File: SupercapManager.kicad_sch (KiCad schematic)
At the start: 7 parts, among them J1 JST4_M, J2 XT30_M, J3 XT30_M, J4 XT30_M, J5 XT30_M, Q11 BSC015NE2LS5I, Q12 BSC015NE2LS5I

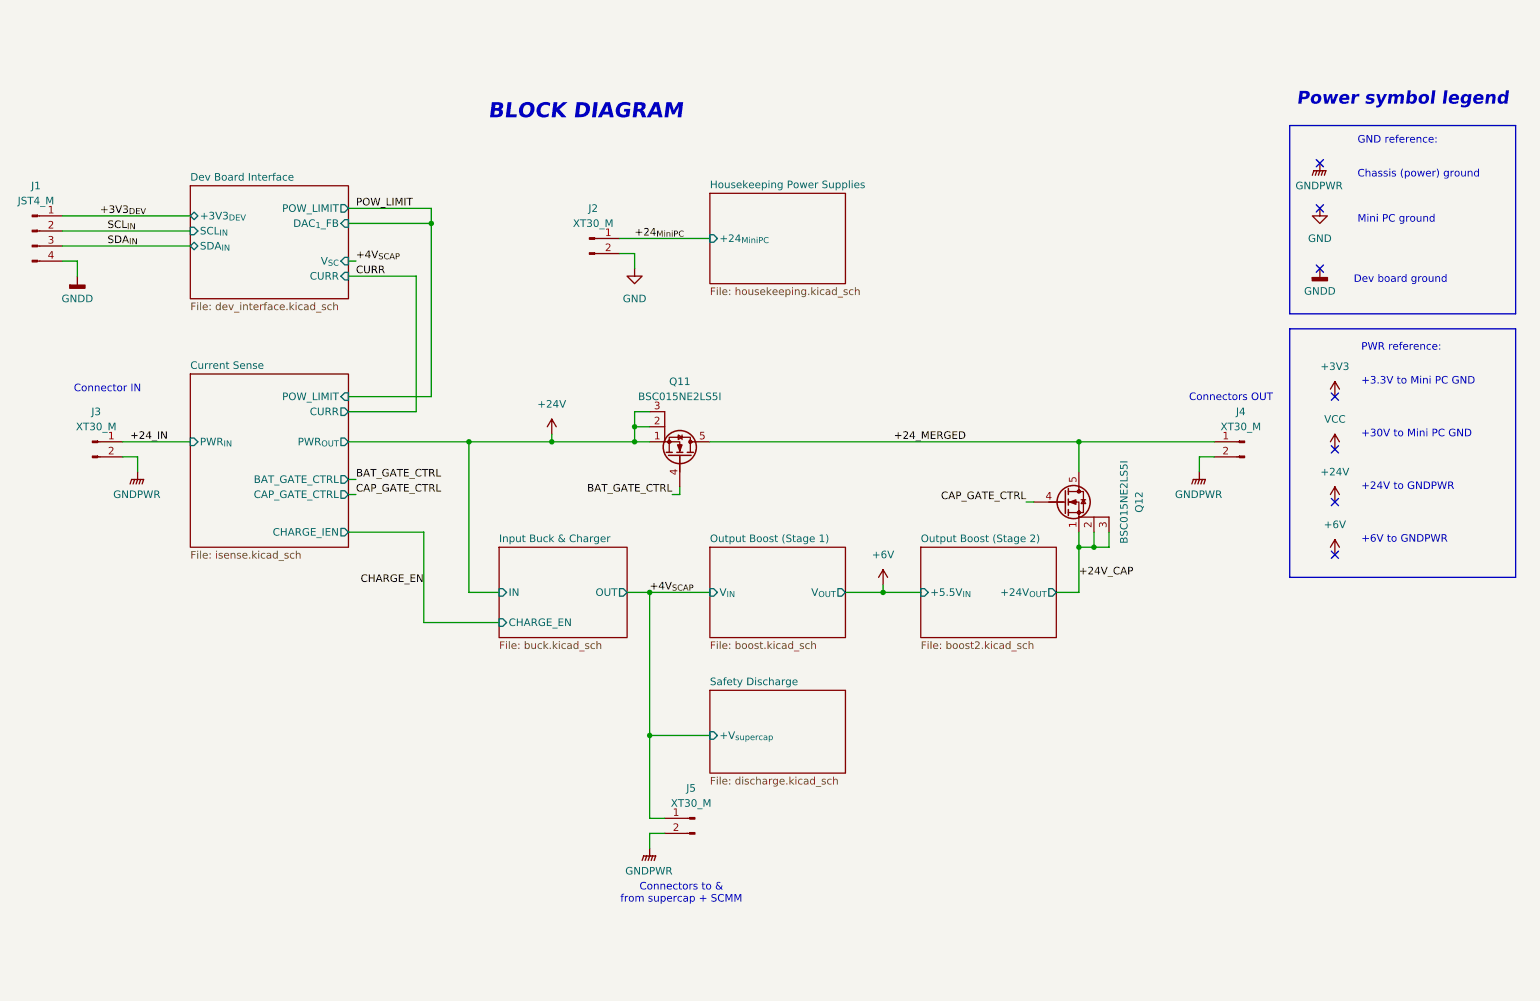
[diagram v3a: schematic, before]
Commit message: Up charging current to 6A
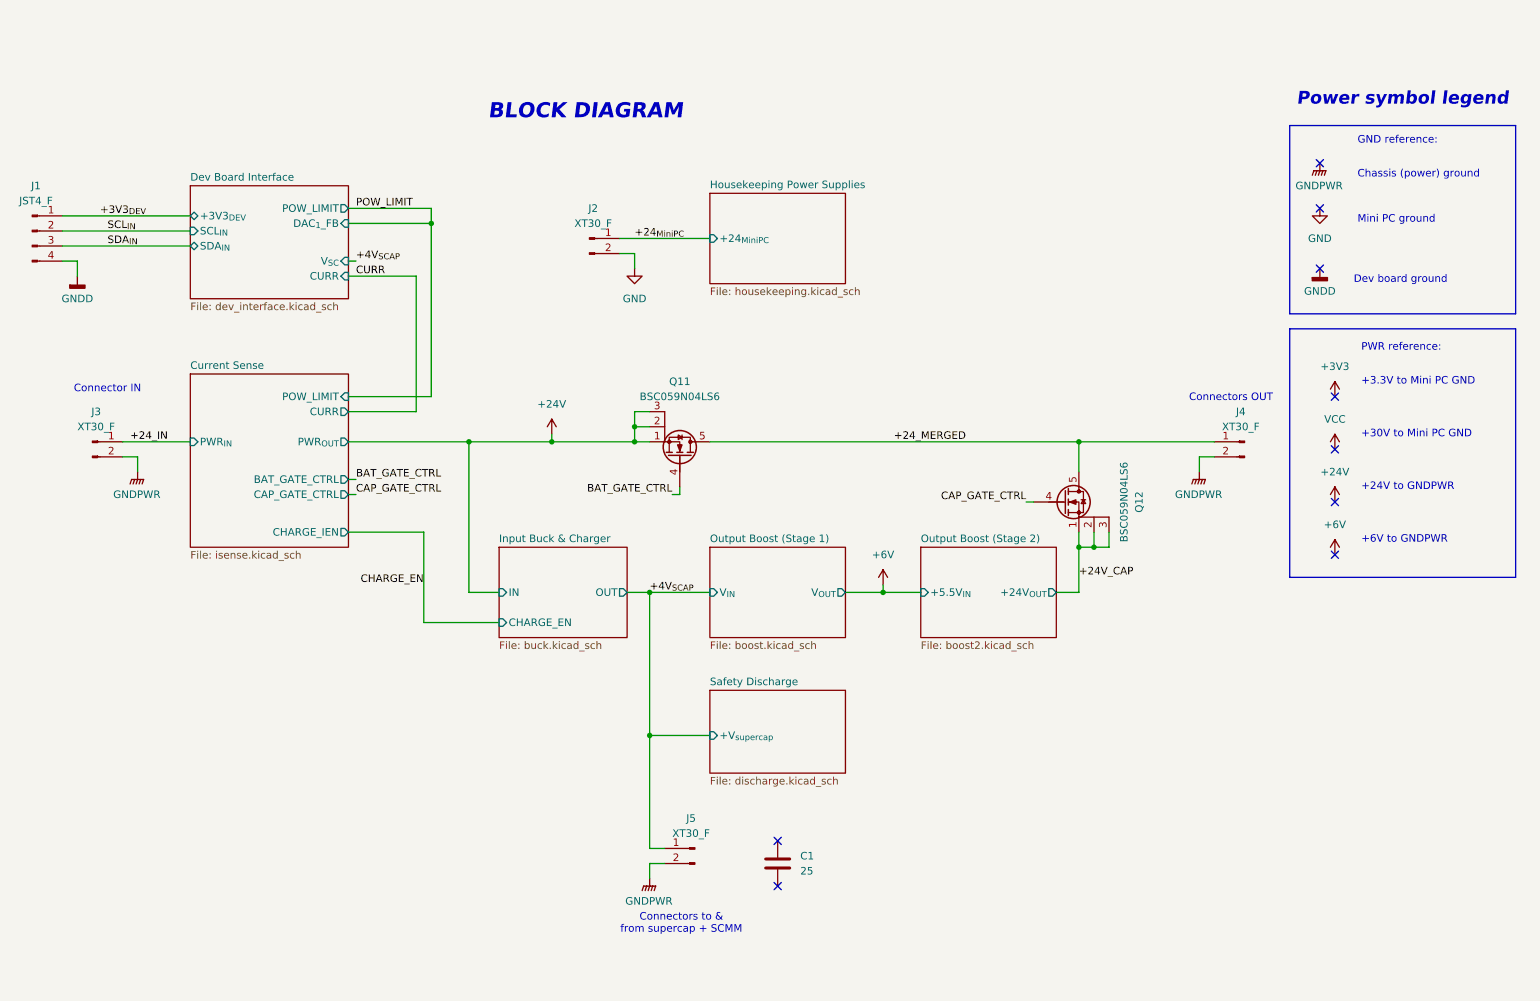
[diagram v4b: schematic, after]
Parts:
- added C1: 25, symbol Device:C
- J1: value JST4_M -> JST4_F
- J2, J3, J4, J5: value XT30_M -> XT30_F; footprint Connector_AMASS:AMASS_XT30U-M_1x02_P5.0mm_Vertical -> Connector_AMASS:AMASS_XT30U-F_1x02_P5.0mm_Vertical
- Q11, Q12: value BSC015NE2LS5I -> BSC059N04LS6; Mouser Part Number 726-BSC015NE2LS5IATM -> 726-BSC059N04LS6ATMA
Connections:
- no-connect marks 7 -> 9
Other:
- moved on the sheet: J5
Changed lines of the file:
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@@
 	(text "Connectors to &\nfrom supercap + SCMM"
 		(exclude_from_sim no)
-		(at 131.064 168.402 0)
+		(at 131.064 173.482 0)
 		(effects
 			(font
@@
 	)
 	(no_connect
+		(at 147.32 161.29)
+	)
+	(no_connect
 		(at 241.3 86.36)
+	)
+	(no_connect
+		(at 147.32 168.91)
 	)
 	(no_connect
@@
 	(wire
 		(pts
-			(xy 128.27 160.02) (xy 125.73 160.02)
+			(xy 128.27 165.1) (xy 125.73 165.1)
 		)
 		(stroke
@@
 	(wire
 		(pts
-			(xy 125.73 157.48) (xy 125.73 143.51)
+			(xy 125.73 162.56) (xy 125.73 143.51)
 		)
 		(stroke
@@
 	(wire
 		(pts
-			(xy 128.27 157.48) (xy 125.73 157.48)
+			(xy 128.27 162.56) (xy 125.73 162.56)
 		)
 		(stroke
@@
 	(wire
 		(pts
-			(xy 125.73 160.02) (xy 125.73 162.56)
+			(xy 125.73 165.1) (xy 125.73 167.64)
 		)
 		(stroke
@@
 			)
 		)
-		(property "Value" "BSC015NE2LS5I"
+		(property "Value" "BSC059N04LS6"
 			(at 130.81 86.36 90)
 			(effects
@@
 			)
 		)
-		(property "Mouser Part Number" "726-BSC015NE2LS5IATM"
+		(property "Mouser Part Number" "726-BSC059N04LS6ATMA"
 			(at 130.81 96.52 0)
 			(effects
@@
 	)
 	(symbol
+		(lib_id "Device:C")
+		(at 147.32 165.1 0)
+		(unit 1)
+		(exclude_from_sim no)
+		(in_bom yes)
+		(on_board no)
+		(dnp no)
+		(fields_autoplaced yes)
+		(property "Reference" "C1"
+			(at 151.13 163.8299 0)
+			(effects
+				(font
+					(size 1.27 1.27)
+				)
+				(justify left)
+			)
+		)
+		(property "Value" "25"
+			(at 151.13 166.3699 0)
+			(effects
+				(font
+					(size 1.27 1.27)
+				)
+				(justify left)
+			)
+		)
+		(property "Footprint" ""
+			(at 148.2852 168.91 0)
+			(effects
+				(font
+					(size 1.27 1.27)
+				)
+				(hide yes)
+			)
+		)
+		(property "Datasheet" "https://www.mouser.com/datasheet/2/40/AVX_SCC-3084824.pdf"
+			(at 147.32 165.1 0)
+			(effects
+				(font
+					(size 1.27 1.27)
+				)
+				(hide yes)
+			)
+		)
+		(property "Description" "Supercapacitor"
+			(at 147.32 165.1 0)
+			(effects
+				(font
+					(size 1.27 1.27)
+				)
+				(hide yes)
+			)
+		)
+		(property "Mouser Part Number" "581-SCCU25B256SRB"
+			(at 147.32 165.1 0)
+			(effects
+				(font
+					(size 1.27 1.27)
+				)
+				(hide yes)
+			)
+		)
+		(pin "1"
+		)
+		(pin "2"
+		)
+		(instances
+			(project ""
+				(path "/6197145b-e7d4-44cc-9d90-537b6501bf60"
+					(reference "C1")
+					(unit 1)
+				)
+			)
+		)
+	)
+	(symbol
 		(lib_id "power:VCC")
 		(at 241.3 95.25 0)
@@
 	(symbol
 		(lib_id "Connector:Conn_01x02_Pin")
-		(at 133.35 157.48 0)
+		(at 133.35 162.56 0)
 		(mirror y)
 		(unit 1)
@@
 		(dnp no)
 		(property "Reference" "J5"
-			(at 132.715 152.4 0)
-			(effects
-				(font
-					(size 1.27 1.27)
-				)
-			)
-		)
-		(property "Value" "XT30_M"
-			(at 132.715 154.94 0)
-			(effects
-				(font
-					(size 1.27 1.27)
-				)
-			)
-		)
-		(property "Footprint" "Connector_AMASS:AMASS_XT30U-M_1x02_P5.0mm_Vertical"
-			(at 133.35 157.48 0)
+			(at 132.715 157.48 0)
+			(effects
+				(font
+					(size 1.27 1.27)
+				)
+			)
+		)
+		(property "Value" "XT30_F"
+			(at 132.715 160.02 0)
+			(effects
+				(font
+					(size 1.27 1.27)
+				)
+			)
+		)
+		(property "Footprint" "Connector_AMASS:AMASS_XT30U-F_1x02_P5.0mm_Vertical"
+			(at 133.35 162.56 0)
 			(effects
 				(font
@@
 		)
 		(property "Datasheet" "~"
-			(at 133.35 157.48 0)
+			(at 133.35 162.56 0)
 			(effects
 				(font
@@
 		)
 		(property "Description" "Generic connector, single row, 01x02, script generated"
-			(at 133.35 157.48 0)
+			(at 133.35 162.56 0)
 			(effects
 				(font
@@
 		)
 		(property "Sim.Device" ""
-			(at 133.35 157.48 0)
+			(at 133.35 162.56 0)
 			(effects
 				(font
@@
 		)
 		(property "Sim.Pins" ""
-			(at 133.35 157.48 0)
+			(at 133.35 162.56 0)
 			(effects
 				(font
@@
 		)
 		(property "Sim.Type" ""
-			(at 133.35 157.48 0)
+			(at 133.35 162.56 0)
 			(effects
 				(font
@@
 		)
 		(property "Height" ""
-			(at 133.35 157.48 0)
+			(at 133.35 162.56 0)
 			(effects
 				(font
@@
 		)
 		(property "Manufacturer_Name" ""
-			(at 133.35 157.48 0)
+			(at 133.35 162.56 0)
 			(effects
 				(font
@@
 		)
 		(property "Manufacturer_Part_Number" ""
-			(at 133.35 157.48 0)
+			(at 133.35 162.56 0)
 			(effects
 				(font
@@
 		)
 		(property "Mouser Price/Stock" ""
-			(at 133.35 157.48 0)
+			(at 133.35 162.56 0)
 			(effects
 				(font
@@
 	(symbol
 		(lib_id "power:GNDPWR")
-		(at 125.73 162.56 0)
+		(at 125.73 167.64 0)
 		(unit 1)
 		(exclude_from_sim no)
@@
 		(fields_autoplaced yes)
 		(property "Reference" "#PWR014"
+			(at 125.73 172.72 0)
+			(effects
+				(font
+					(size 1.27 1.27)
+				)
+				(hide yes)
+			)
+		)
+		(property "Value" "GNDPWR"
+			(at 125.603 171.45 0)
+			(effects
+				(font
+					(size 1.27 1.27)
+				)
+			)
+		)
+		(property "Footprint" ""
+			(at 125.73 168.91 0)
+			(effects
+				(font
+					(size 1.27 1.27)
+				)
+				(hide yes)
+			)
+		)
+		(property "Datasheet" ""
+			(at 125.73 168.91 0)
+			(effects
+				(font
+					(size 1.27 1.27)
+				)
+				(hide yes)
+			)
+		)
+		(property "Description" "Power symbol creates a global label with name \"GNDPWR\" , global ground"
 			(at 125.73 167.64 0)
-			(effects
-				(font
-					(size 1.27 1.27)
-				)
-				(hide yes)
-			)
-		)
-		(property "Value" "GNDPWR"
-			(at 125.603 166.37 0)
-			(effects
-				(font
-					(size 1.27 1.27)
-				)
-			)
-		)
-		(property "Footprint" ""
-			(at 125.73 163.83 0)
-			(effects
-				(font
-					(size 1.27 1.27)
-				)
-				(hide yes)
-			)
-		)
-		(property "Datasheet" ""
-			(at 125.73 163.83 0)
-			(effects
-				(font
-					(size 1.27 1.27)
-				)
-				(hide yes)
-			)
-		)
-		(property "Description" "Power symbol creates a global label with name \"GNDPWR\" , global ground"
-			(at 125.73 162.56 0)
 			(effects
 				(font
@@
 			)
 		)
-		(property "Value" "XT30_M"
+		(property "Value" "XT30_F"
 			(at 116.205 57.15 0)
 			(effects
@@
 			)
 		)
-		(property "Footprint" "Connector_AMASS:AMASS_XT30U-M_1x02_P5.0mm_Vertical"
+		(property "Footprint" "Connector_AMASS:AMASS_XT30U-F_1x02_P5.0mm_Vertical"
 			(at 115.57 59.69 0)
 			(effects
@@
 			)
 		)
-		(property "Value" "XT30_M"
+		(property "Value" "XT30_F"
 			(at 32.385 91.44 0)
 			(effects
@@
 			)
 		)
-		(property "Footprint" "Connector_AMASS:AMASS_XT30U-M_1x02_P5.0mm_Vertical"
+		(property "Footprint" "Connector_AMASS:AMASS_XT30U-F_1x02_P5.0mm_Vertical"
 			(at 31.75 93.98 0)
 			(effects
@@
 			)
 		)
-		(property "Value" "BSC015NE2LS5I"
+		(property "Value" "BSC059N04LS6"
 			(at 205.74 104.14 90)
 			(effects
@@
 			)
 		)
-		(property "Mouser Part Number" "726-BSC015NE2LS5IATM"
+		(property "Mouser Part Number" "726-BSC059N04LS6ATMA"
 			(at 195.58 104.14 0)
 			(effects
@@
 			)
 		)
-		(property "Value" "JST4_M"
+		(property "Value" "JST4_F"
 			(at 22.225 53.34 0)
 			(effects
@@
 			)
 		)
-		(property "Value" "XT30_M"
+		(property "Value" "XT30_F"
 			(at 225.425 91.44 0)
 			(effects
@@
 			)
 		)
-		(property "Footprint" "Connector_AMASS:AMASS_XT30U-M_1x02_P5.0mm_Vertical"
+		(property "Footprint" "Connector_AMASS:AMASS_XT30U-F_1x02_P5.0mm_Vertical"
 			(at 226.06 93.98 0)
 			(effects

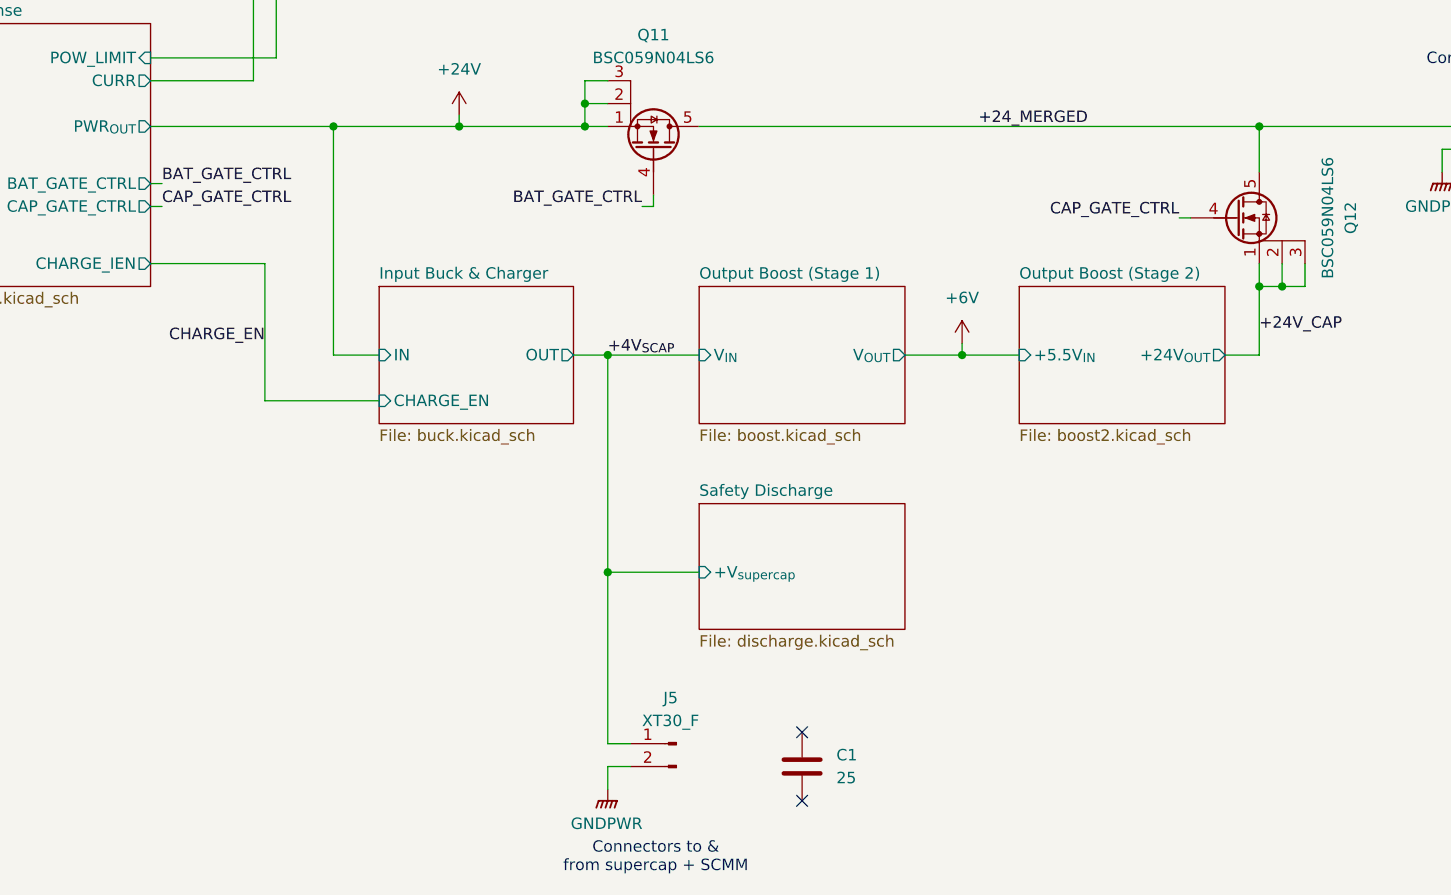
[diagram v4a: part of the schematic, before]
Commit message: Add supercaps subsheets
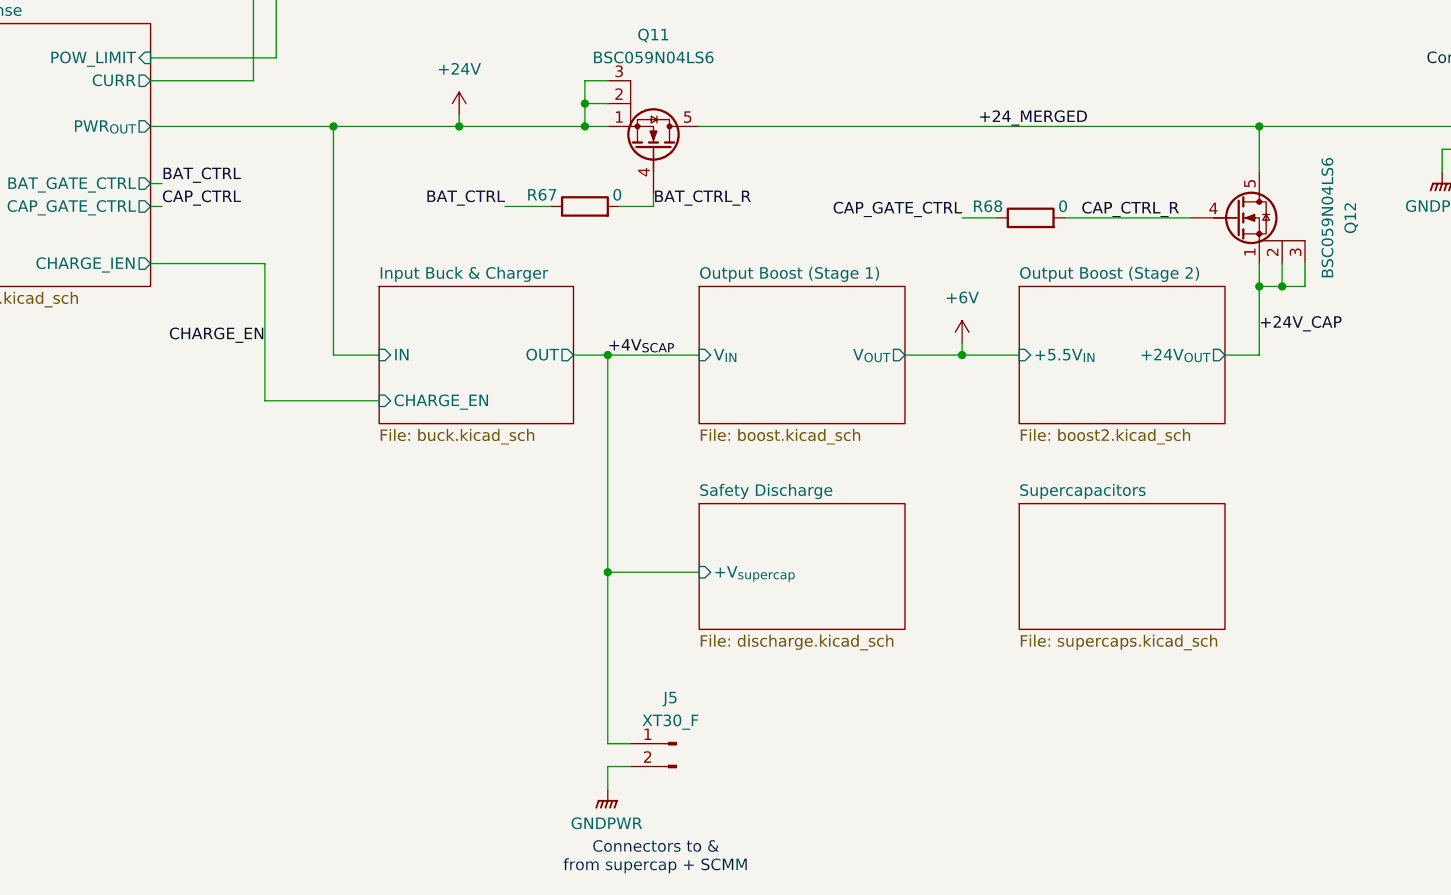
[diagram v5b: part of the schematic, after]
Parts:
- removed C1: 25, symbol Device:C
- added R67, R68: 0, Resistor_SMD:R_0603_1608Metric_Pad0.98x0.95mm_HandSolder, symbol Device:R
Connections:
- net CAP_GATE_CTRL: now also R68.1; no longer Q12.4 (G)
- net BAT_GATE_CTRL renamed BAT_CTRL_R
- net BAT_CTRL_R: now also R67.2
- new net BAT_CTRL: R67.1
- new net CAP_CTRL_R: Q12.4 (G), R68.2
- no-connect marks 9 -> 7
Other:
- added sheet Supercapacitors (supercaps.kicad_sch)
